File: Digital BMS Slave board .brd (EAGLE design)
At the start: 105.4 x 100 mm, 268 parts, among them J1 S7B-PH-K, J10 S3B-PH-K, J11 S4B-PH-K, J2 S4B-PH-K, J3 S4B-PH-K, J4 S6B-PH-K, J5 S2B-PH-K, J6 S2B-PH-K, J7 S2B-PH-K, J8 S2B-PH-K, J9 S3B-PH-K, Q1 BSS123, Q2 BSS123, Q3 BSS123, Q4 BSS123, Q5 BSS123, Q6 BSS123, U1 BQ79606A-Q1-HTQFP(PHP)|48, X2 PESD2CAN, X3 PESD2CAN, X4 PESD2CAN, X5 PESD2CAN

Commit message: components placed on board
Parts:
- removed JP4: 1x7, commonly used connectors:1X07
- removed JP5: 2x7, pinhead:2X07
- removed TP14, TP18, TP19, TP20, TP21, TP22, TP23, TP24, TP25, TP26, TP27, TP28, TP29, TP33: TEST_PAD2, testing:TP1.27MM_MASK
- removed TP30, TP31, TP32, TP34, TP35, TP36, TP37, TP39, TP41, TP44, TP45, TP46, TP47, TP48, TP49, TP50: TEST_PAD, testing:TP1MM_MASK
- added J12: S4B-PH-K, con-jst-ph:S4B-PH-K
- J1: value S7B-PH-K -> S4B-PH-K; device con-jst-ph:B7B-PH-K -> con-jst-ph:S4B-PH-K
- TP1, TP10, TP11, TP12, TP15, TP16, TP17, TP3, TP4, TP5, TP6, TP7, TP8, TP9: value TEST_PAD2 -> TEST_PAD; device testing:TP1.27MM_MASK -> testing:TP1MM_MASK
- TP13: value TEST_PAD2 -> TEST_PAD1; device testing:TP1.27MM_MASK -> testing:TP1MM_NOMASK
- U1: value BQ79606A-Q1-HTQFP(PHP)|48 -> BQ79606A-Q1-[HTQFP(PHP)|48]; device texas Instrumets:QFP50P900X900X105-49T500 -> texas Instrumets:HTQFP48-9X9MM
- moved D9 186.7 mm to (50.1, 14.5)
- moved TP70 184.1 mm to (62.7, 29.5), turned to 90 degrees
- moved R44 180.7 mm to (46.3, 14.5), turned to 180 degrees
- moved TP69 180.3 mm to (64.5, 29.5), turned to 90 degrees
- moved TP68 176.5 mm to (66.4, 29.5), turned to 90 degrees
- moved J11 174.5 mm to (3.36, 30.6), flipped to the bottom, turned to 90 degrees
- moved TP67 172.8 mm to (68.2, 29.5), turned to 90 degrees
- moved R74 169.9 mm to (49.8, 6.83), turned to 90 degrees
- moved TP66 169.2 mm to (70.0, 29.5), turned to 90 degrees
- moved TP65 165.7 mm to (71.8, 29.5), turned to 90 degrees
- moved TP63 162.9 mm to (98.1, 16.6)
- moved TP64 161.6 mm to (87.8, 18.6)
- moved TP58 149.5 mm to (97.9, 23.0)
- moved TP60 143.7 mm to (86.0, 16.8)
- moved TP61 141.0 mm to (73.7, 18.7)
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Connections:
- net 123 renamed SB1
- net 1234 renamed SB0
- net BAT105 renamed SB4
- net BAT59 renamed SB5
- net BAT65 renamed SB3
- net BAT75 renamed SB2
- net N$1 renamed BAT
- net N$2 renamed LDOIN
- net N$29 renamed EB4
- net N$32 renamed EB5
- net N$35 renamed CL1_N
- net N$36 renamed CL1_P
- net N$37 renamed FL1_N
- net N$38 renamed FL1_P
- net N$4 renamed EB6
- net N$41 renamed FL_N
- net N$42 renamed FL_P
- net N$43 renamed CL_N
- net N$44 renamed CL_P
- net N$47 renamed FH1_N
- net N$48 renamed FH1_P
- net N$5 renamed DVDD
- net N$51 renamed FH2_P
- net N$52 renamed FH2_N
- net N$53 renamed CH1_N
- net N$54 renamed CH1_P
- net N$57 renamed CH2_P
- net N$58 renamed CH2_N
- net N$64 renamed EB3
- net N$67 renamed EB2
- net N$7 renamed VPROG
- net N$72 renamed EB1
- net N$75 renamed EB0
- net N$83 renamed VC1
- net VCC15 renamed SB6
- removed net COMHN: C53.2, R39.1, R43.1, TP14.1, U1.21
- removed net COMHP: C52.2, R39.2, R42.1, TP13.1, U1.22
- removed net COMLN: C36.2, R13.1, R9.1, TP10.1, U1.20
- removed net COMLP: C35.2, R12.1, R9.2, TP9.1, U1.19
- removed net FAULTHN: C49.2, R14.1, R38.1, TP12.1, U1.23
- removed net FAULTHP: C39.2, R14.2, R37.1, TP11.1, U1.24
- removed net FAULTLN: C8.2, R3.1, R8.1, TP4.1, U1.18
- removed net FAULTLP: C5.2, R3.2, R7.1, TP3.1, U1.17
- removed net ISO_COMHN: J3.4, L4.3, TP17.1
- removed net ISO_COMHP: J3.3, L4.4, TP18.1
- removed net ISO_COMLN: J2.4, L2.3, TP7.1
- removed net ISO_COMLP: J2.3, L2.4, TP8.1
- removed net ISO_FAULTHN: J3.2, L3.3, TP16.1
- removed net ISO_FAULTHP: J3.1, L3.4, TP15.1
- removed net ISO_FAULTN: J2.2, L1.3, TP6.1
- removed net ISO_FAULTP: J2.1, L1.4, TP5.1
- removed net N$13: C26.1, C27.2, C28.2, R24.2, TP24.1, U1.4
- removed net N$14: C41.1, C42.2, C43.2, JP5.4, R31.2
- removed net N$15: C29.1, C30.2, R26.2, TP22.1, U1.8
- removed net N$16: C30.1, C31.2, C32.2, R27.2, TP21.1, U1.10
- removed net N$17: C27.1, C28.1, C29.2, R25.2, TP23.1, U1.6
- removed net N$18: C33.1, C40.2, R29.2, TP20.1, U1.14
- removed net N$26: C26.2, R23.2, TP25.1, U1.2
- removed net N$33: C60.1, C62.2, JP4.2, R48.2, R49.2, TP66.1
- removed net N$39: C34.1, L1.1
- removed net N$40: C13.1, L1.2
- removed net N$45: C38.1, L2.1
- removed net N$46: C37.1, L2.2
- removed net N$49: R16.1, R38.2, X3.2
- removed net N$50: R15.1, R37.2, X3.1
- removed net N$55: R41.1, R43.2, X4.2
- removed net N$56: R40.1, R42.2, X4.1
- removed net N$6: C60.2, JP4.1, R100.2, TP65.1
- removed net N$61: C62.1, C64.2, JP4.3, R51.2, R52.2, TP67.1
- removed net N$65: C64.1, C66.2, JP4.4, R53.2, R54.2, TP68.1
- removed net N$66: C66.1, C68.2, JP4.5, R55.2, R56.2, TP69.1
- removed net N$69: C44.1, C45.2, JP5.8, R33.2
- removed net N$73: C68.1, C70.2, JP4.6, R57.2, R58.2, TP70.1
- removed net N$74: C70.1, JP4.7, R59.2, R60.2
- removed net N$77: C48.1, C55.2, JP5.14, R36.2
- removed net N$78: C41.2, JP5.2, R30.2
- removed net N$79: C46.1, C47.1, C48.2, JP5.12, R35.2
- removed net N$80: C45.1, C46.2, C47.2, JP5.10, R34.2
- removed net N$81: C42.1, C43.1, C44.2, JP5.6, R32.2
- new net 4: J12.4
- new net CH_N: R41.1, R43.2, X4.1
- new net CH_P: R40.1, R42.2, X4.2
- new net CL2_N: C37.1, L2.1
- new net CL2_P: C38.1, L2.2
- new net COMH_N: C53.2, R39.1, R43.1, TP8.1, U1.21
- new net COMH_P: C52.2, R39.2, R42.1, TP15.1, U1.22
- new net COML_N: C36.2, R13.1, R9.1, TP1.1, U1.20
- new net COML_P: C35.2, R12.1, R9.2, TP5.1, U1.19
- new net FAULTH_N: C49.2, R14.1, R38.1, TP16.1, U1.23
- new net FAULTH_P: C39.2, R14.2, R37.1, TP17.1, U1.24
- new net FAULTL_N: C8.2, R3.1, R8.1, TP6.1, U1.18
- new net FAULTL_P: C5.2, R3.2, R7.1, TP7.1, U1.17
- new net FH_N: R16.1, R38.2, X3.1
- new net FH_P: R15.1, R37.2, X3.2
- new net FL2_N: C13.1, L1.1
- new net FL2_P: C34.1, L1.2
- new net ISO_COMH_N: J3.4, L4.3
- new net ISO_COMH_P: J3.3, L4.4
- new net ISO_COML_N: J2.1, L2.4
- new net ISO_COML_P: J2.2, L2.3
- new net ISO_FAULTH_N: J3.2, L3.3
- new net ISO_FAULTH_P: J3.1, L3.4
- new net ISO_FAULTL_N: J2.3, L1.4
- new net ISO_FAULTL_P: J2.4, L1.3
- new net VC0: C33.1, C40.2, R29.2, TP3.1, U1.14
- new net VC2: C30.1, C31.2, C32.2, R27.2, TP4.1, U1.10
- new net VC3: C29.1, C30.2, R26.2, TP9.1, U1.8
- new net VC4: C27.1, C28.1, C29.2, R25.2, TP10.1, U1.6
- new net VC5: C26.1, C27.2, C28.2, R24.2, TP11.1, U1.4
- new net VC6: C26.2, R23.2, TP12.1, U1.2
- net BAT1: now also J12.3; no longer J1.2, TP1.1
- net BAT2: now also J1.2; no longer J1.3, TP19.1
- net BAT3: now also J12.2; no longer J1.4, TP26.1
- net BAT4: now also J1.3; no longer J1.5, TP27.1
- net BAT5: now also J12.1; no longer J1.6, TP28.1
- net CB0: now also C48.1, C55.2, C70.1, R36.2, R59.2, R60.2, TP13.1; no longer JP5.13
- net CB1: now also C46.1, C47.1, C48.2, C68.1, C70.2, R35.2, R57.2, R58.2, TP70.1; no longer JP5.11
- net CB2: now also C45.1, C46.2, C47.2, C66.1, C68.2, R34.2, R55.2, R56.2, TP69.1; no longer JP5.9
- net CB3: now also C44.1, C45.2, C64.1, C66.2, R33.2, R53.2, R54.2, TP68.1; no longer JP5.7
- net CB4: now also C42.1, C43.1, C44.2, C62.1, C64.2, R32.2, R51.2, R52.2, TP67.1; no longer JP5.5
- net CB5: now also C41.1, C42.2, C43.2, C60.1, C62.2, R31.2, R48.2, R49.2, TP66.1; no longer JP5.3
- net CB6: now also C41.2, C60.2, R100.2, R30.2, TP65.1; no longer JP5.1
- net GND: no longer TP33.1, TP36.1, TP47.1, TP50.1
- net GPIO4: now also JP1.8; no longer JP1.12
- net GPIO6: now also JP1.12; no longer JP1.8
- net N$10: no longer TP37.1
- net N$11: no longer TP39.1
- net N$25: no longer TP46.1
- net N$27: no longer TP49.1
- net N$8: no longer TP41.1
- net N$9: no longer TP44.1
- net NFAULT: no longer TP35.1
- net RX1: no longer TP32.1
- net TSREF: no longer TP45.1, TP48.1
- net TX: no longer TP31.1
- net VCC: now also J1.4; no longer J1.7, TP29.1
- net VIO: no longer TP30.1
- net WAKEUP: no longer TP34.1
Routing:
- net GND: track 0.00 -> 26.8 mm, vias 0 -> 2
- net EB1: track 0.00 -> 18.3 mm
- net TX: track 0.00 -> 15.6 mm, vias 0 -> 1
- net RX: track 0.00 -> 14.9 mm, vias 0 -> 1
- net NFAULT: track 0.00 -> 13.9 mm, vias 0 -> 1
- net VCC: track 0.00 -> 10.9 mm
- net EB2: track 0.00 -> 9.84 mm
- net VIO: track 0.00 -> 9.57 mm
- net N$71: track 0.00 -> 9.13 mm
- net N$63: track 0.00 -> 8.47 mm
- net VPROG: track 0.00 -> 7.07 mm
- net TSREF: track 0.00 -> 5.96 mm
- net EB0: track 0.00 -> 4.95 mm
- net LDOIN: track 0.00 -> 3.73 mm
- net N$34: track 0.00 -> 3.22 mm
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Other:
- board size 105.4 x 100 mm -> 100 x 60 mm
- board text added: "Ferrite"

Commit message: Go home
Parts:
- TP1, TP10, TP11, TP12, TP15, TP16, TP17, TP2, TP3, TP38, TP4, TP40, TP42, TP43, TP5, TP51, TP52, TP6, TP7, TP8, TP9: value TEST_PAD -> TEST_PAD-[1MM]
- TP13, TP53, TP54, TP55, TP56, TP57, TP58, TP59, TP60, TP61, TP62, TP63, TP64, TP65, TP66, TP67, TP68, TP69, TP70: value TEST_PAD1 -> TEST_PAD-[1.27MM]; device testing:TP1MM_NOMASK -> testing:TP1.27MM
- moved D9 9.63 mm to (40.6, 13.2)
- moved R44 9.44 mm to (37.0, 13.1)
- moved C2 6.38 mm to (25.3, 17.3), turned to 90 degrees
- moved C3 6.06 mm to (31.9, 17.4)
- moved C12 5.15 mm to (22.9, 17.5)
- moved R6 5.15 mm to (20.8, 17.5)
- moved R2 3.87 mm to (38.5, 17.4)
- moved C1 3.62 mm to (40.7, 17.3), turned to 90 degrees
- moved C11 2.50 mm to (24.9, 21.6)
- moved C4 1.91 mm to (36.4, 17.4)
- moved C6 1.21 mm to (33.9, 17.4)
- moved TP16 0.91 mm to (26.3, 32.8)
- moved TP5 0.91 mm to (34.4, 32.7)
- moved TP7 0.87 mm to (38.5, 32.7)
- moved TP17 0.85 mm to (25.1, 32.8)
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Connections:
- new net PAD: U1.49
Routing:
- net FAULTH_P: track 0.00 -> 10.1 mm
- net FAULTH_N: track 0.00 -> 8.98 mm
- net VCC: track 10.9 -> 2.46 mm
- net FAULTL_N: track 0.00 -> 6.30 mm
- net FAULTL_P: track 0.00 -> 6.26 mm
- net VPROG: track 7.07 -> 11.8 mm
- net BAT: track 0.00 -> 4.72 mm
- net COMH_P: track 0.00 -> 3.75 mm
- net WAKEUP: track 0.00 -> 3.55 mm, vias 0 -> 1
- net COMH_N: track 0.00 -> 3.25 mm
- net AVDD: track 2.76 -> 4.87 mm, vias 0 -> 1
- net REF1: track 2.09 -> 3.97 mm
- net RX: track 14.9 -> 13.1 mm
- net TSREF: track 5.96 -> 4.22 mm
- net TX: track 15.6 -> 13.9 mm
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- added copper zone on layer 15, net GND
- added copper zone on layer 16, net GND
- added copper zone on layer 2, net GND
- added copper zone on layer 15, net VCC

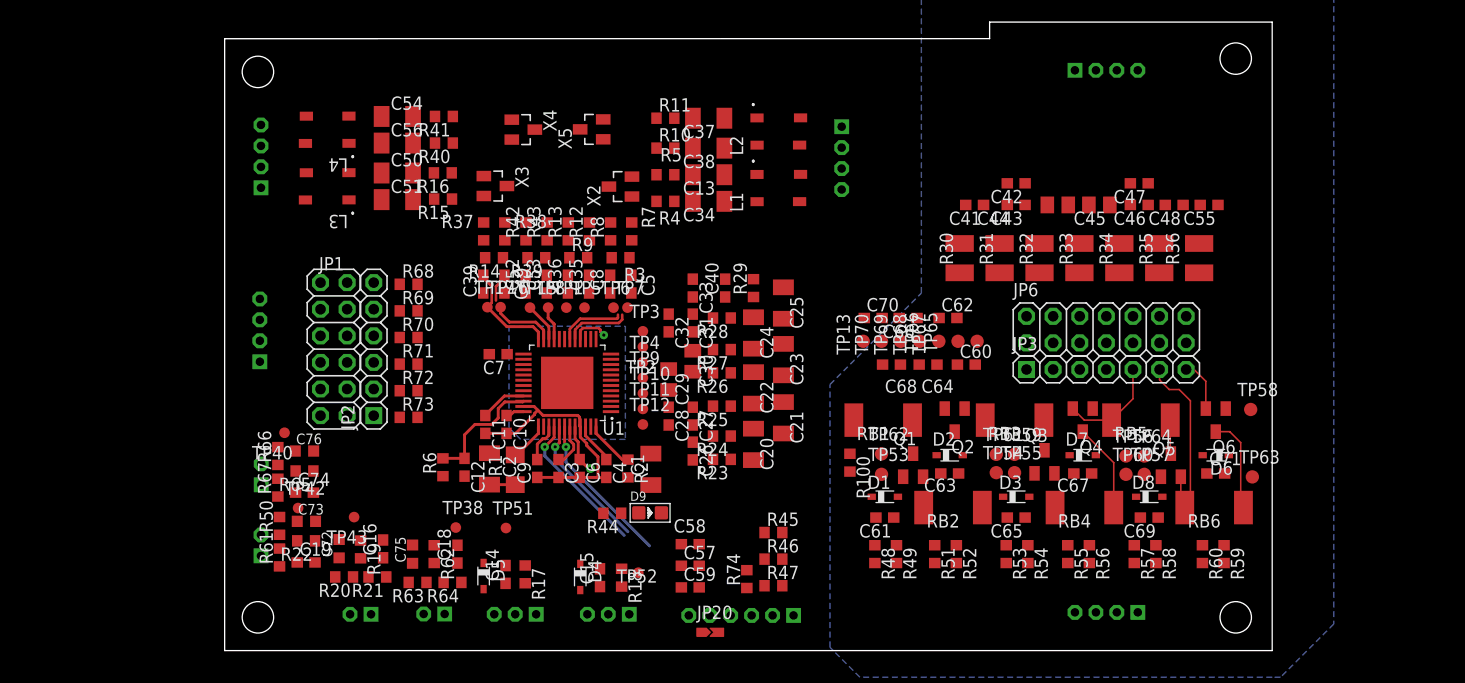
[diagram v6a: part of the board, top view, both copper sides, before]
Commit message: COM and IC CAP routed
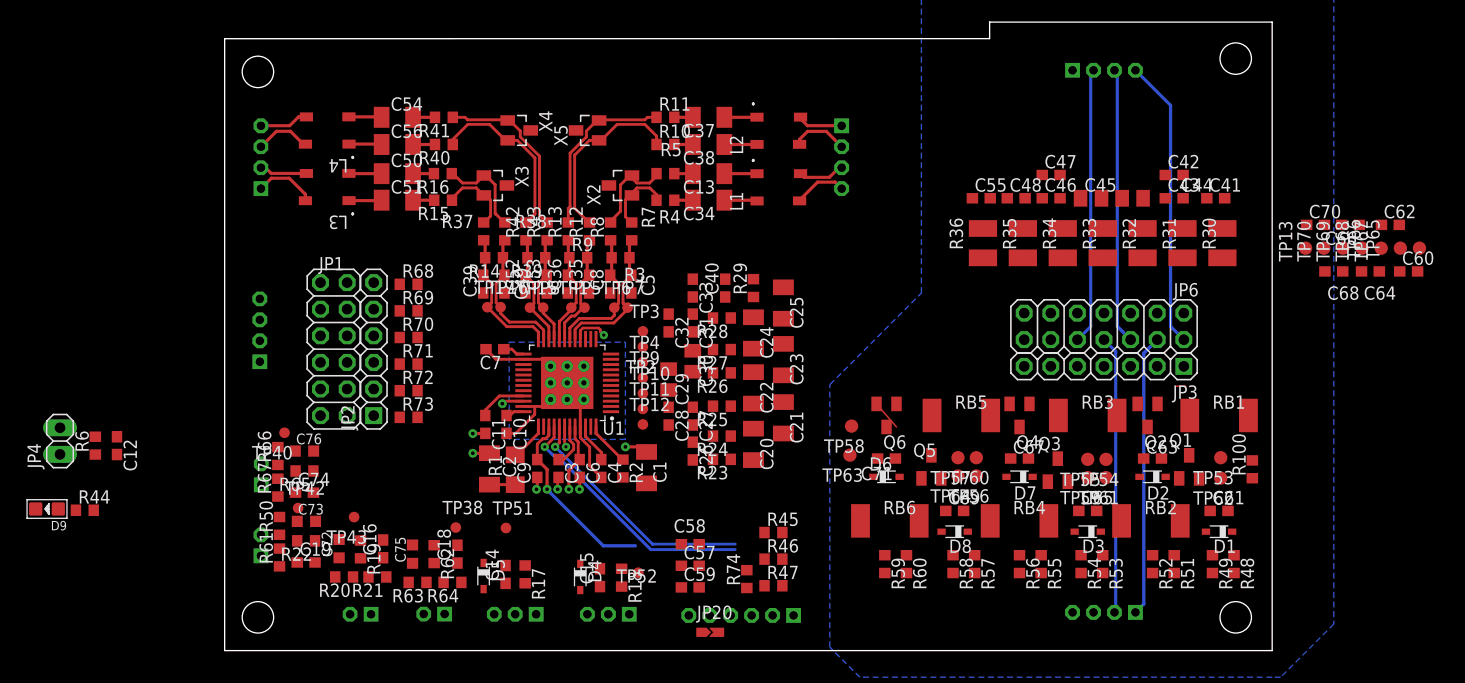
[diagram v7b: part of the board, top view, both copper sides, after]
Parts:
- added JP4: (no value), pinhead:1X02
- U1: value BQ79606A-Q1-[HTQFP(PHP)|48] -> BQ79606A-Q1-HTQFP|48|9VIA; device texas Instrumets:HTQFP48-9X9MM -> texas Instrumets:HTQFP48-9X9MM-VIA
- moved D9 57.6 mm to (-17.0, 13.5), turned to 180 degrees
- moved R44 50.4 mm to (-13.3, 13.4), turned to 0 degrees
- moved C60 43.2 mm to (113.0, 36.2)
- moved C68 43.2 mm to (105.9, 36.2)
- moved TP65 43.2 mm to (114.1, 38.4)
- moved TP69 43.2 mm to (106.8, 38.4)
- moved TP70 43.2 mm to (104.9, 38.4)
- moved C70 43.2 mm to (104.1, 40.6)
- moved TP13 43.2 mm to (103.2, 38.4)
- moved C62 43.2 mm to (111.3, 40.6)
- moved C64 43.2 mm to (109.4, 36.2)
- moved C66 43.2 mm to (107.5, 40.6)
- moved TP66 43.2 mm to (112.2, 38.4)
- moved TP67 43.2 mm to (110.4, 38.4)
- moved TP68 43.2 mm to (108.6, 38.4)
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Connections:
- removed net PAD: U1.49
- new net N$2: JP4.2, R6.2
- net BAT1: now also JP6.12; no longer JP6.11
- net BAT2: now also JP6.10; no longer JP6.9
- net BAT3: now also JP6.8; no longer JP6.7
- net BAT4: now also JP6.6; no longer JP6.5
- net BAT5: now also JP6.4; no longer JP6.3
- net GND: now also JP6.14, U1.49, U1.491, U1.492, U1.493, U1.494, U1.495, U1.496, U1.497, U1.498, U1.499; no longer JP6.13
- net SB0: now also JP6.13; no longer JP6.14
- net SB1: now also JP6.11; no longer JP6.12
- net SB2: now also JP6.9; no longer JP6.10
- net SB3: now also JP6.7; no longer JP6.8
- net SB4: now also JP6.5; no longer JP6.6
- net SB5: now also JP6.3; no longer JP6.4
- net SB6: now also JP6.1; no longer JP6.2
- net VCC: now also JP6.2; no longer JP6.1
- net VPROG: now also JP4.1; no longer R6.2
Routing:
- net VCC: track 2.46 -> 30.1 mm
- net BAT5: track 0.00 -> 26.9 mm
- net BAT3: track 0.00 -> 26.5 mm
- net BAT2: track 0.00 -> 26.4 mm
- net BAT4: track 0.00 -> 26.4 mm
- net CL_P: track 0.00 -> 17.3 mm
- net CH_N: track 0.00 -> 16.8 mm
- net CH_P: track 0.00 -> 16.8 mm
- net CL_N: track 0.00 -> 16.7 mm
- net VIO: track 8.21 -> 24.5 mm, vias 0 -> 1
- net EB1: track 18.3 -> 3.36 mm
- net NFAULT: track 14.7 -> 1.99 mm
- net COML_P: track 0.00 -> 11.1 mm
- net TX: track 13.9 -> 24.5 mm
- net COML_N: track 0.00 -> 10.6 mm
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- added copper zone on layer 1, net GND
- removed copper zone on layer 15, net VCC

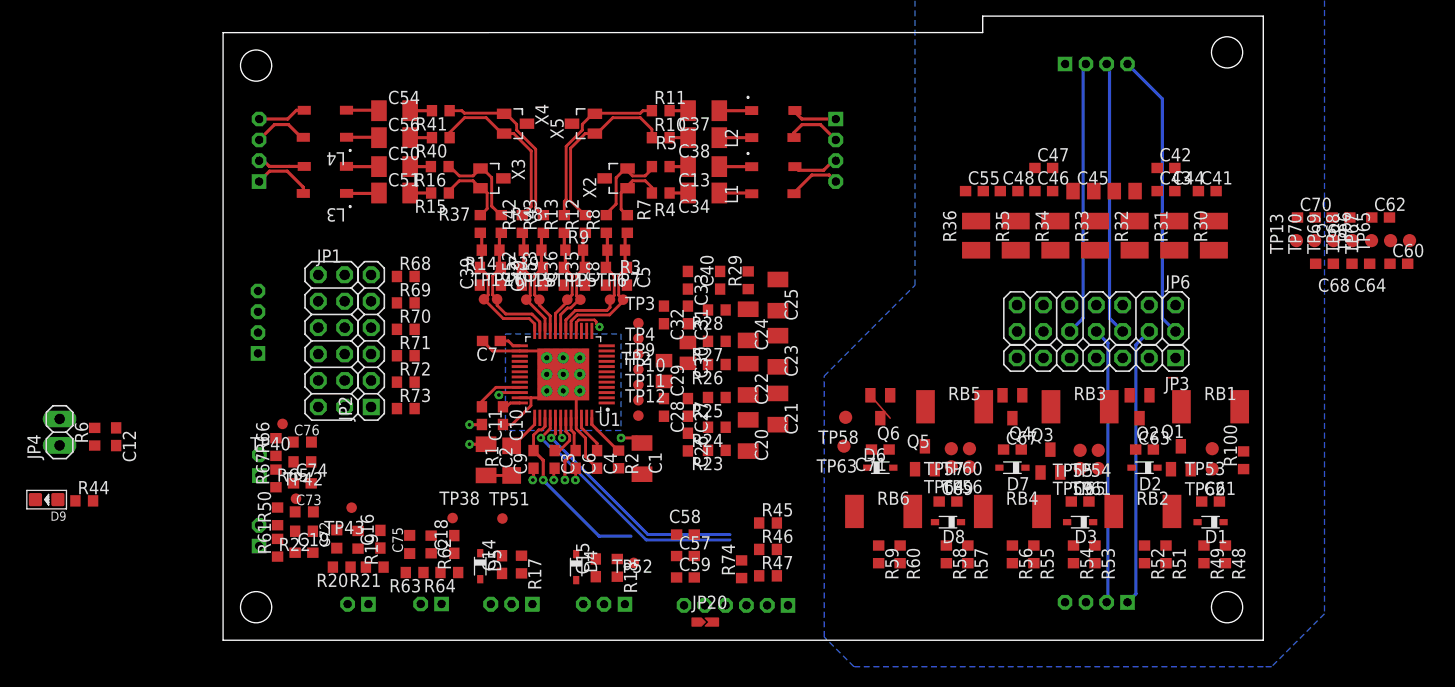
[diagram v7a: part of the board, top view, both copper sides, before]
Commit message: GPIO routed
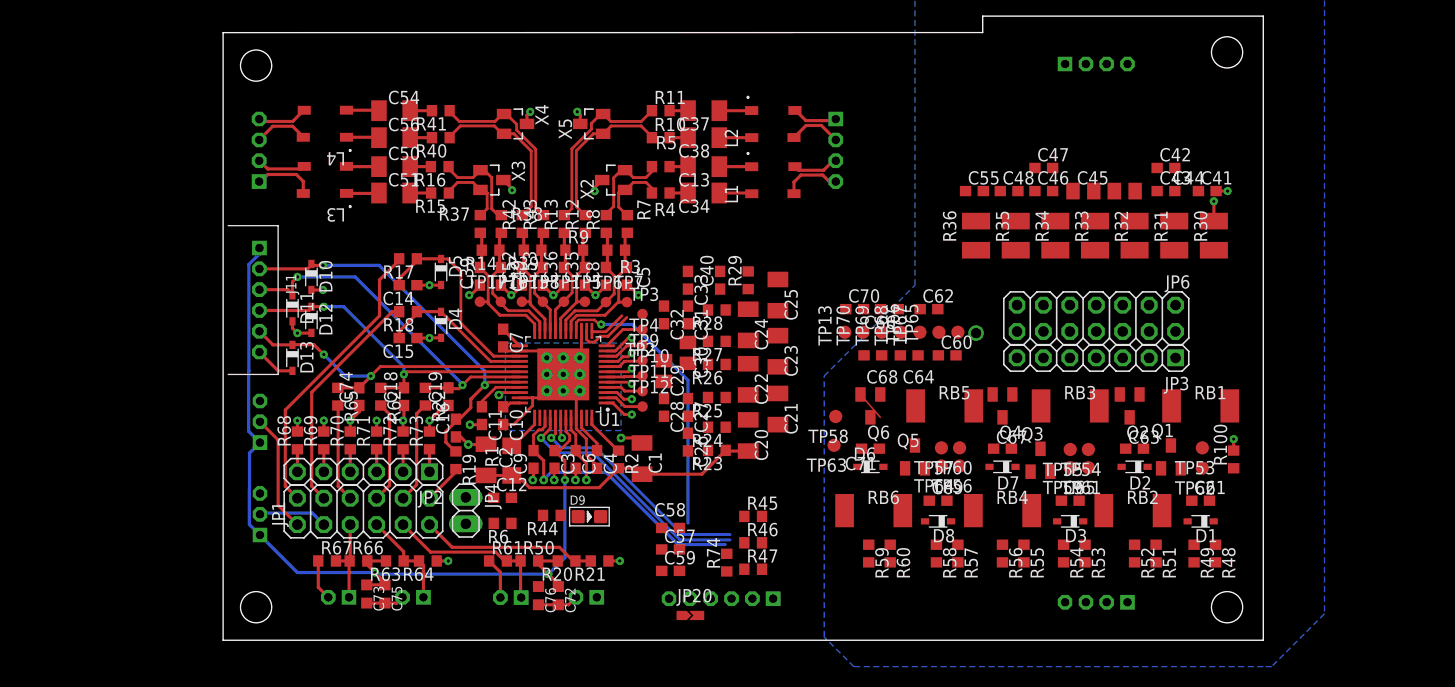
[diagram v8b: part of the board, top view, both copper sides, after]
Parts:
- removed TP38, TP40, TP42, TP43, TP51, TP52: TEST_PAD-[1MM], testing:TP1MM_MASK
- added D10, D11, D12, D13: 6.2V, Semiconductor_devices:SOD323_ST
- J11: value S4B-PH-K -> S6B-PH-K; device con-jst-ph:S4B-PH-K -> con-jst-ph:S6B-PH-K
- moved D9 52.2 mm to (35.2, 11.9), turned to 0 degrees
- moved R44 45.0 mm to (31.6, 12.0), turned to 180 degrees
- moved C60 44.3 mm to (69.6, 27.4)
- moved C62 44.3 mm to (67.9, 31.8)
- moved C64 44.3 mm to (66.0, 27.4)
- moved C68 44.3 mm to (62.5, 27.4)
- moved C70 44.3 mm to (60.7, 31.8)
- moved TP13 44.3 mm to (59.8, 29.6)
- moved TP65 44.3 mm to (70.6, 29.6)
- moved TP66 44.3 mm to (68.8, 29.6)
- moved TP69 44.3 mm to (63.3, 29.6)
- moved TP70 44.3 mm to (61.5, 29.6)
- moved C66 44.3 mm to (64.1, 31.8)
- moved TP67 44.3 mm to (67.0, 29.6)
- moved TP68 44.3 mm to (65.2, 29.6)
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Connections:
- removed net N$10: J6.1, R62.2, R63.1, R64.2
- removed net N$11: J7.1, R65.2, R66.1, R67.2
- removed net N$25: J10.2, R17.2
- removed net N$27: J9.2, R18.2
- removed net N$8: J8.1, R22.2, R50.1, R61.2
- removed net N$9: J5.1, R19.2, R20.1, R21.2
- new net GPIO1F: JP1.2, R17.2
- new net GPIO2F: JP1.4, R18.2
- new net GPIO3F: JP1.6, R65.2
- new net GPIO4F: JP1.8, R62.2
- new net GPIO5F: JP1.10, R22.2
- new net GPIO6F: JP1.12, R19.2
- net GND: now also D10.A, D11.A, D12.A, D13.A, J11.6
- net GPIO1: now also C14.2, D5.C, R17.1; no longer JP1.2
- net GPIO1V2: now also J10.2; no longer C14.2, D5.C, R17.1, TP51.1
- net GPIO2: now also C15.2, D4.C, R18.1; no longer JP1.4
- net GPIO2V1: now also J9.2; no longer C15.2, D4.C, R18.1, TP52.1
- net GPIO3: now also C74.2, D13.C, J11.5, R65.1; no longer J11.4, JP1.6
- net GPIO3T4: now also J7.1, R66.1, R67.2; no longer C74.2, R65.1, TP40.1
- net GPIO4: now also C18.2, D12.C, J11.4, R62.1; no longer J11.3, JP1.8
- net GPIO4T3: now also J6.1, R63.1, R64.2; no longer C18.2, R62.1, TP38.1
- net GPIO5: now also C19.2, D11.C, J11.3, R22.1; no longer J11.2, JP1.10
- net GPIO5T2: now also J8.1, R50.1, R61.2; no longer C19.2, R22.1, TP42.1
- net GPIO6: now also C16.2, D10.C, J11.2, R19.1; no longer J11.1, JP1.12
- net GPIO6T1: now also J5.1, R20.1, R21.2; no longer C16.2, R19.1, TP43.1
- net TSREF: now also J11.1
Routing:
- net GND: track 31.6 -> 120.3 mm, vias 6 -> 27
- net TSREF: track 4.22 -> 88.4 mm, vias 0 -> 3
- net GPIO6: track 0.00 -> 39.6 mm, vias 0 -> 2
- net GPIO5: track 0.00 -> 35.2 mm, vias 0 -> 2
- net GPIO4: track 0.00 -> 32.0 mm, vias 0 -> 2
- net GPIO3: track 0.00 -> 30.9 mm, vias 0 -> 2
- net BAT1: track 0.00 -> 28.6 mm
- net GPIO1F: track 0.00 -> 28.0 mm
- net VCC: track 30.1 -> 55.3 mm
- net WAKEUP: track 3.55 -> 27.8 mm
- net GPIO2F: track 0.00 -> 22.3 mm
- net GPIO1: track 0.00 -> 19.9 mm
- net GPIO6T1: track 0.00 -> 16.9 mm
- net GPIO5T2: track 0.00 -> 16.5 mm
- net GPIO2: track 0.00 -> 15.1 mm
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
